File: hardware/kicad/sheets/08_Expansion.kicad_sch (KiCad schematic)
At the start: 23 parts, among them U801 TLV841S fixed 2.7 V; 10 ms de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, U802 Dual-supply I2C hot-swap buff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

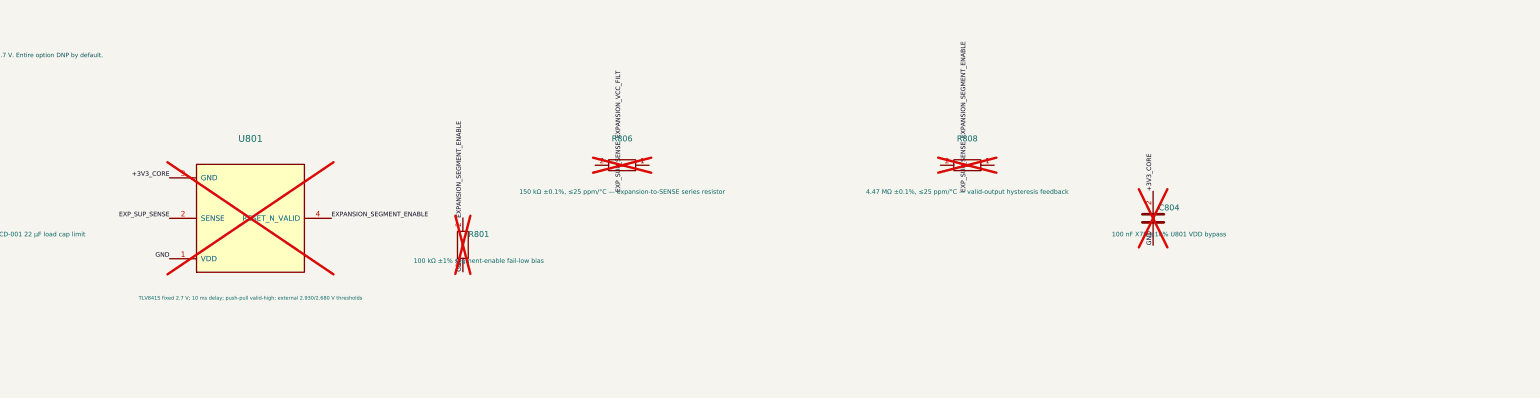
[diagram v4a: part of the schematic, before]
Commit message: Remediate power active device compatibility
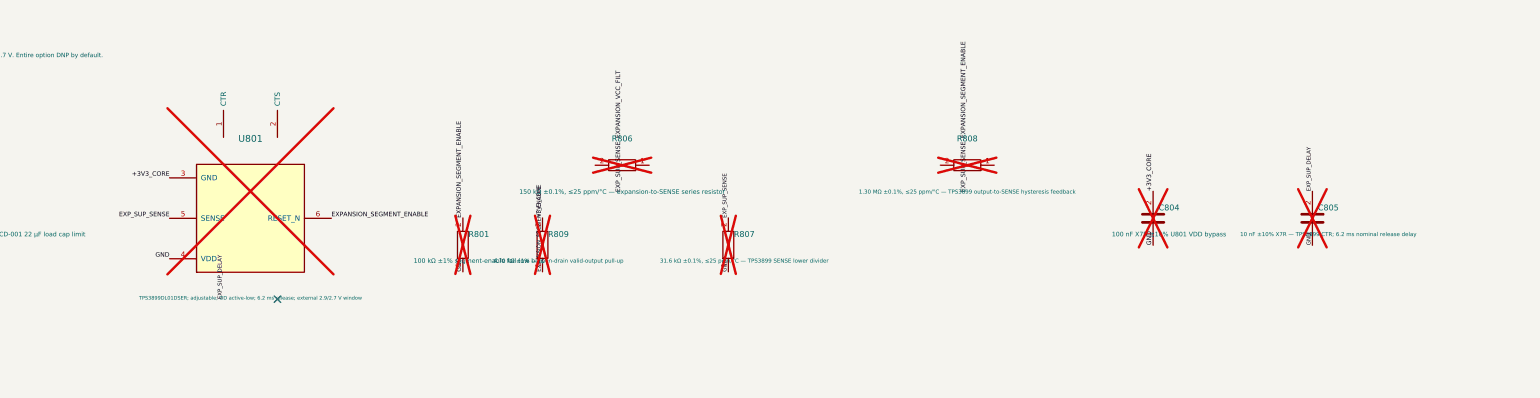
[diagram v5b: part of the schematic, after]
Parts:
- added C805: 10 nF ±10% X7R — TPS3899 CTR; 6.2 ms nominal rele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, symbol IPC100:C
- added R807: 31.6 kΩ ±0.1%, ≤25 ppm/°C — TPS3899 SENSE lower d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, symbol IPC100:R
- added R809: 4.70 kΩ ±1% — open-drain valid-output pull-up, symbol IPC100:R
- R808: value 4.47 MΩ ±0.1%, ≤25 ppm/°C — valid-output hysteresis feedback -> 1.30 MΩ ±0.1%, ≤25 ppm/°C — TPS3899 output-to-SENSE hysteresis feedback
- U801: value TLV841S fixed 2.7 V; 10 ms delay; push-pull valid-high; external 2.930/2.680 V thresholds -> TPS3899DL01DSER; adjustable; OD active-low; 6.2 ms release; external 2.9/2.7 V window; symbol IPC100:TLV841S_2V7_VALID_HIGH -> IPC100:TPS3899DL01
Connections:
- net +3V3_CORE: now also R809.2
- net EXPANSION_SEGMENT_ENABLE: now also U801.6 (RESET_N), R809.1; no longer U801.4 (RESET_N_VALID)
- net EXP_SUP_SENSE: now also U801.5 (SENSE), R807.2; no longer U801.2 (SENSE)
- net GND: now also U801.4 (VDD), C805.1, R807.1; no longer U801.1 (VDD)
- new net EXP_SUP_DELAY: C805.2
- no-connect marks 0 -> 1
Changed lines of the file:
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@@
   (label "EXPANSION_VCC_FILT" (at 110 49.92 90) (effects (font (size 0.85 0.85)) (justify left bottom)))
   (label "GND" (at 110 60.08 90) (effects (font (size 0.85 0.85)) (justify left bottom)))
-  (symbol (lib_id "IPC100:TLV841S_2V7_VALID_HIGH") (at 165 55 0) (unit 1) (exclude_from_sim no) (in_bom yes) (on_board yes) (dnp yes)
+  (symbol (lib_id "IPC100:TPS3899DL01") (at 165 55 0) (unit 1) (exclude_from_sim no) (in_bom yes) (on_board yes) (dnp yes)
     (property "Reference" "U801" (at 165 40 0) (effects (font (size 1.27 1.27))))
-    (property "Value" "TLV841S fixed 2.7 V; 10 ms delay; push-pull valid-high; external 2.930/2.680 V thresholds" (at 165 70 0) (effects (font (size 0.68 0.68))))
-    (property "Footprint" "" (at 165 55 0) (effects (font (size 1 1)) hide)) (property "Datasheet" "https://www.ti.com/lit/ds/symlink/tlv841.pdf" (at 165 55 0) (effects (font (size 1 1)) hide))
+    (property "Value" "TPS3899DL01DSER; adjustable; OD active-low; 6.2 ms release; external 2.9/2.7 V window" (at 165 70 0) (effects (font (size 0.68 0.68))))
+    (property "Footprint" "" (at 165 55 0) (effects (font (size 1 1)) hide)) (property "Datasheet" "https://www.ti.com/lit/ds/symlink/tps3899.pdf" (at 165 55 0) (effects (font (size 1 1)) hide))
     (pin "1") (pin "2")
     (pin "3") (pin "4")
+    (pin "5") (pin "6")
     (instances (project "IPC-100" (path "/10000000-0000-4000-8000-000000000001/10000000-0000-4000-8000-000000000432" (reference "U801") (unit 1))))
   )
@@
   (symbol (lib_id "IPC100:R") (at 300 45 90) (unit 1) (exclude_from_sim no) (in_bom yes) (on_board yes) (dnp yes)
     (property "Reference" "R808" (at 300 40 90) (effects (font (size 1.1 1.1))))
-    (property "Value" "4.47 MΩ ±0.1%, ≤25 ppm/°C — valid-output hysteresis feedback" (at 300 50 90) (effects (font (size 0.85 0.85))))
+    (property "Value" "1.30 MΩ ±0.1%, ≤25 ppm/°C — TPS3899 output-to-SENSE hysteresis feedback" (at 300 50 90) (effects (font (size 0.75 0.75))))
     (property "Footprint" "" (at 300 45 0) (effects (font (size 1 1)) hide)) (property "Datasheet" "" (at 300 45 0) (effects (font (size 1 1)) hide))
     (pin "1") (pin "2")
@@
   (label "+3V3_CORE" (at 335 49.92 90) (effects (font (size 0.85 0.85)) (justify left bottom)))
   (label "GND" (at 335 60.08 90) (effects (font (size 0.85 0.85)) (justify left bottom)))
+  (label "EXP_SUP_DELAY" (at 159.92 70.24 90) (effects (font (size 0.75 0.75)) (justify left bottom)))
+  (no_connect (at 170.08 70.24))
+  (symbol (lib_id "IPC100:R") (at 255 60 0) (unit 1) (exclude_from_sim no) (in_bom yes) (on_board yes) (dnp yes)
+    (property "Reference" "R807" (at 258 58 0) (effects (font (size 1.1 1.1))))
+    (property "Value" "31.6 kΩ ±0.1%, ≤25 ppm/°C — TPS3899 SENSE lower divider" (at 258 63 0) (effects (font (size 0.75 0.75))))
+    (property "Footprint" "" (at 255 60 0) (effects (font (size 1 1)) hide)) (property "Datasheet" "" (at 255 60 0) (effects (font (size 1 1)) hide))
+    (pin "1") (pin "2")
+    (instances (project "IPC-100" (path "/10000000-0000-4000-8000-000000000001/10000000-0000-4000-8000-000000000432" (reference "R807") (unit 1))))
+  )
+  (label "EXP_SUP_SENSE" (at 255 54.92 90) (effects (font (size 0.75 0.75)) (justify left bottom)))
+  (label "GND" (at 255 65.08 90) (effects (font (size 0.75 0.75)) (justify left bottom)))
+  (symbol (lib_id "IPC100:R") (at 220 60 0) (unit 1) (exclude_from_sim no) (in_bom yes) (on_board yes) (dnp yes)
+    (property "Reference" "R809" (at 223 58 0) (effects (font (size 1.1 1.1))))
+    (property "Value" "4.70 kΩ ±1% — open-drain valid-output pull-up" (at 223 63 0) (effects (font (size 0.75 0.75))))
+    (property "Footprint" "" (at 220 60 0) (effects (font (size 1 1)) hide)) (property "Datasheet" "" (at 220 60 0) (effects (font (size 1 1)) hide))
+    (pin "1") (pin "2")
+    (instances (project "IPC-100" (path "/10000000-0000-4000-8000-000000000001/10000000-0000-4000-8000-000000000432" (reference "R809") (unit 1))))
+  )
+  (label "+3V3_CORE" (at 220 54.92 90) (effects (font (size 0.75 0.75)) (justify left bottom)))
+  (label "EXPANSION_SEGMENT_ENABLE" (at 220 65.08 90) (effects (font (size 0.75 0.75)) (justify left bottom)))
+  (symbol (lib_id "IPC100:C") (at 365 55 0) (unit 1) (exclude_from_sim no) (in_bom yes) (on_board yes) (dnp yes)
+    (property "Reference" "C805" (at 368 53 0) (effects (font (size 1.1 1.1))))
+    (property "Value" "10 nF ±10% X7R — TPS3899 CTR; 6.2 ms nominal release delay" (at 368 58 0) (effects (font (size 0.75 0.75))))
+    (property "Footprint" "" (at 365 55 0) (effects (font (size 1 1)) hide)) (property "Datasheet" "" (at 365 55 0) (effects (font (size 1 1)) hide))
+    (pin "1") (pin "2")
+    (instances (project "IPC-100" (path "/10000000-0000-4000-8000-000000000001/10000000-0000-4000-8000-000000000432" (reference "C805") (unit 1))))
+  )
+  (label "EXP_SUP_DELAY" (at 365 49.92 90) (effects (font (size 0.75 0.75)) (justify left bottom)))
+  (label "GND" (at 365 60.08 90) (effects (font (size 0.75 0.75)) (justify left bottom)))
   (text "2 — FAIL-DISABLED SEGMENTED I2C BUFFER (100 kHz; NO CLOCK STRETCHING)" (at 20 95 0) (effects (font (size 1.15 1.15) (bold yes)) (justify left bottom)))
   (text "Dual-supply hot-swap class: high-Z when disabled/unpowered, ≤10 µA powered-off leakage per line, no false-low startup pulse, external stuck-low isolated after disable. Sheet 07 remains sole internal pull-up owner." (at 20 102 0) (effects (font (size 0.82 0.82)) (justify left bottom)))
